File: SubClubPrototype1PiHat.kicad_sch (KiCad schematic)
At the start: 26 parts, among them J1 GPIO, J3 Conn_01x06, J4 Conn_01x03, J5 Conn_01x03, J6 Conn_01x03, J7 Conn_01x03, J8 Conn_01x03, J9 Conn_01x03, Q1 IRLZ44N, U1 CAT24C256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

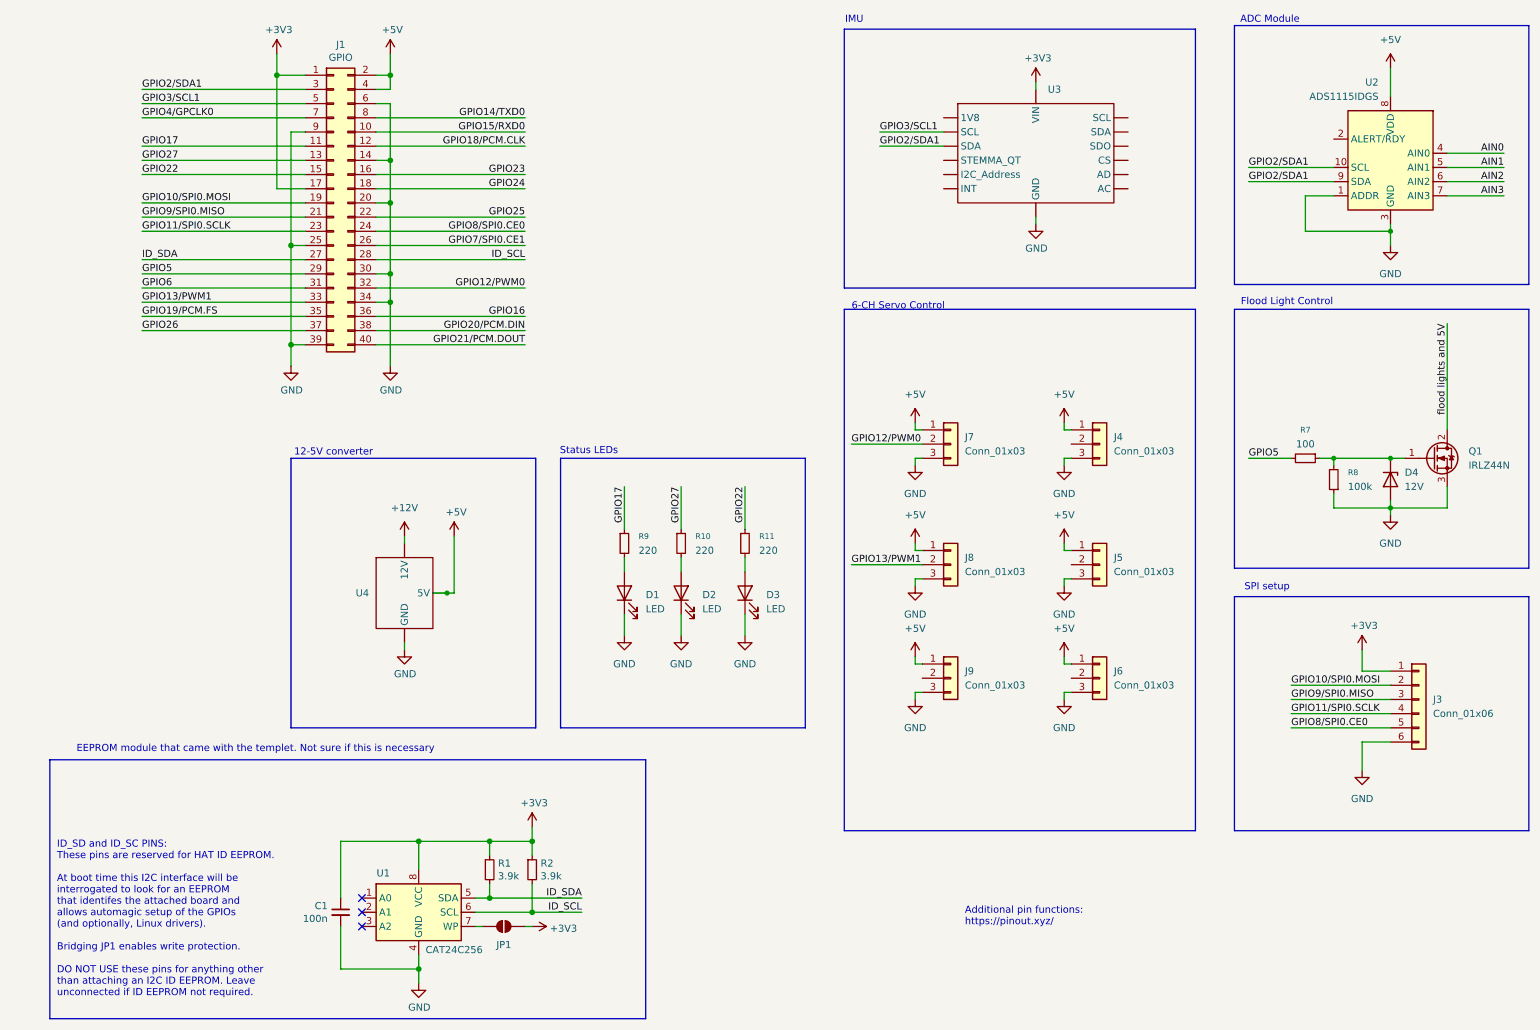
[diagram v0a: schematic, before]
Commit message: deleted EEPROM, servo and ADC
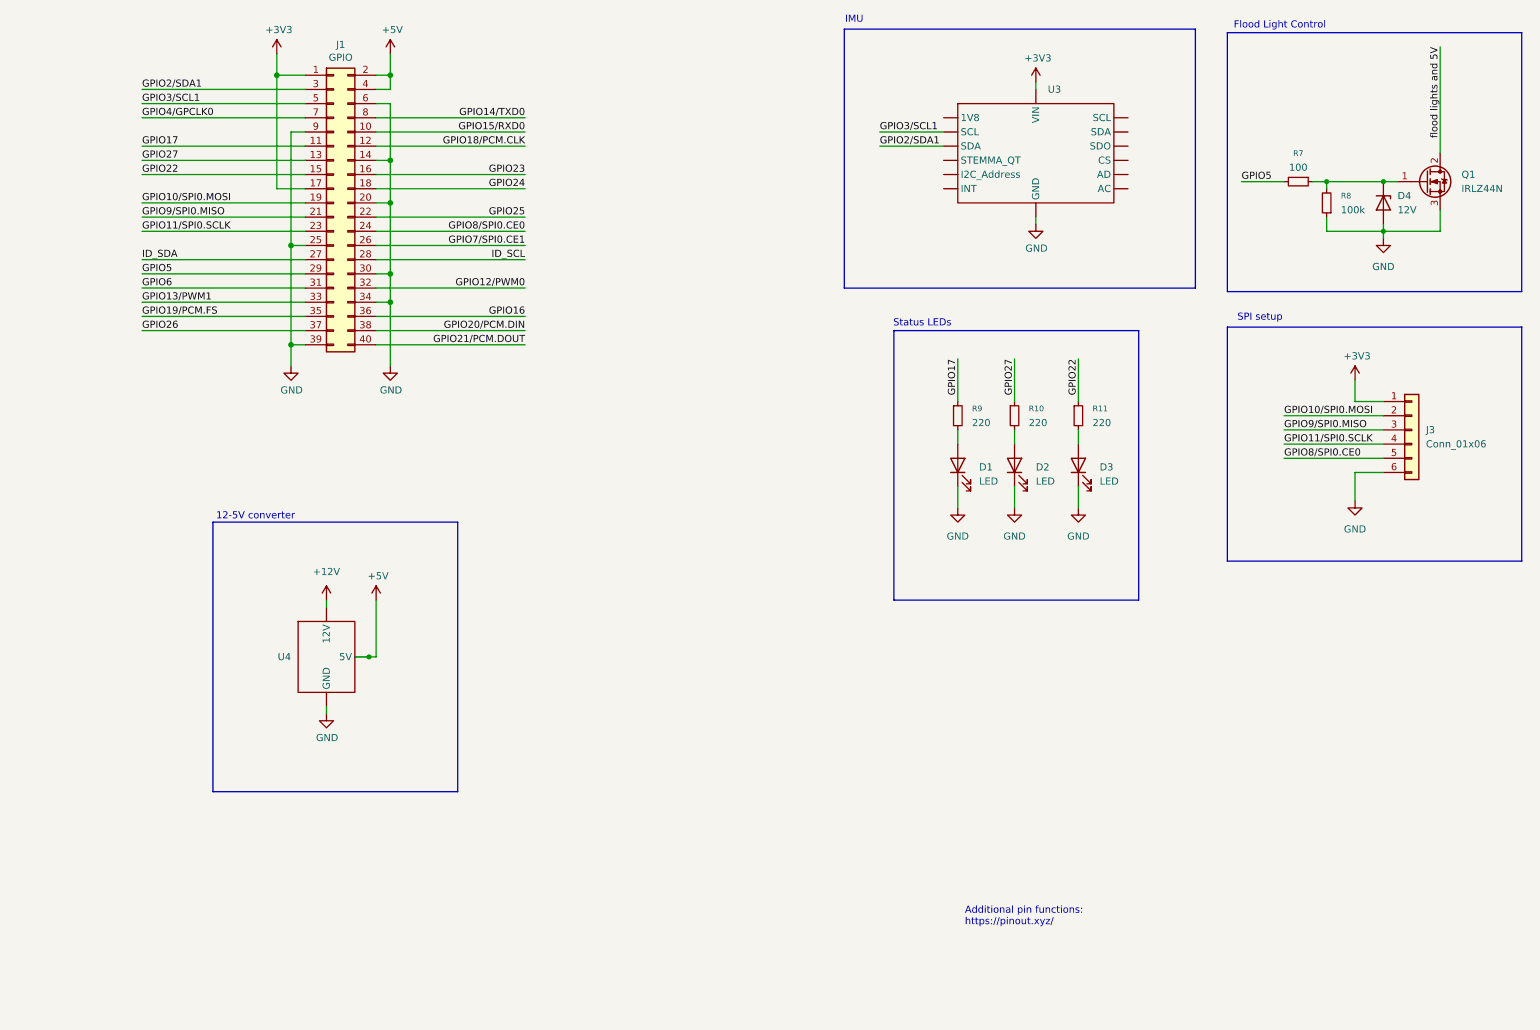
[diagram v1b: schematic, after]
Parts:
- removed C1: 100n, symbol Device:C_Small
- removed J4, J5, J6, J7, J8, J9: Conn_01x03, symbol Connector_Generic:Conn_01x03
- removed JP1: ID_WP, symbol Jumper:SolderJumper_2_Open
- removed R1, R2: 3.9k, symbol Device:R_Small
- removed U1: CAT24C256, symbol Memory_EEPROM:CAT24C256
- removed U2: ADS1115IDGS, Package_SO:TSSOP-10_3x3mm_P0.5mm, symbol Analog_ADC:ADS1115IDGS
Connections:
- no-connect marks 3 -> 0
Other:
- note removed: "6-CH Servo Control"
- note removed: "ADC Module"
- note removed: "EEPROM module that came with the templet. Not sure if this is necessary"
- note removed: "ID_SD and ID_SC PINS: These pins are reserved for HAT ID EEPROM. At boot time this I2C interface will be interrogated to look for an EEPROM that identifes the attached board and allows automagic setup of the GPIOs (and optionally, Linux drivers). Bridging JP1 enables write protection. DO NOT USE these pins for anything other than attaching an I2C ID EEPROM. Leave unconnected if ID EEPROM not requ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"
- title: (none) -> Prototype 1 Pi Hat
- moved on the sheet: D1, D2, D3, D4, J3, Q1, R10, R11, R7, R8, R9, U4
